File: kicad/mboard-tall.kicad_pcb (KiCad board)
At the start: 2 copper layers, 50.8 x 25.4 mm, 10 parts

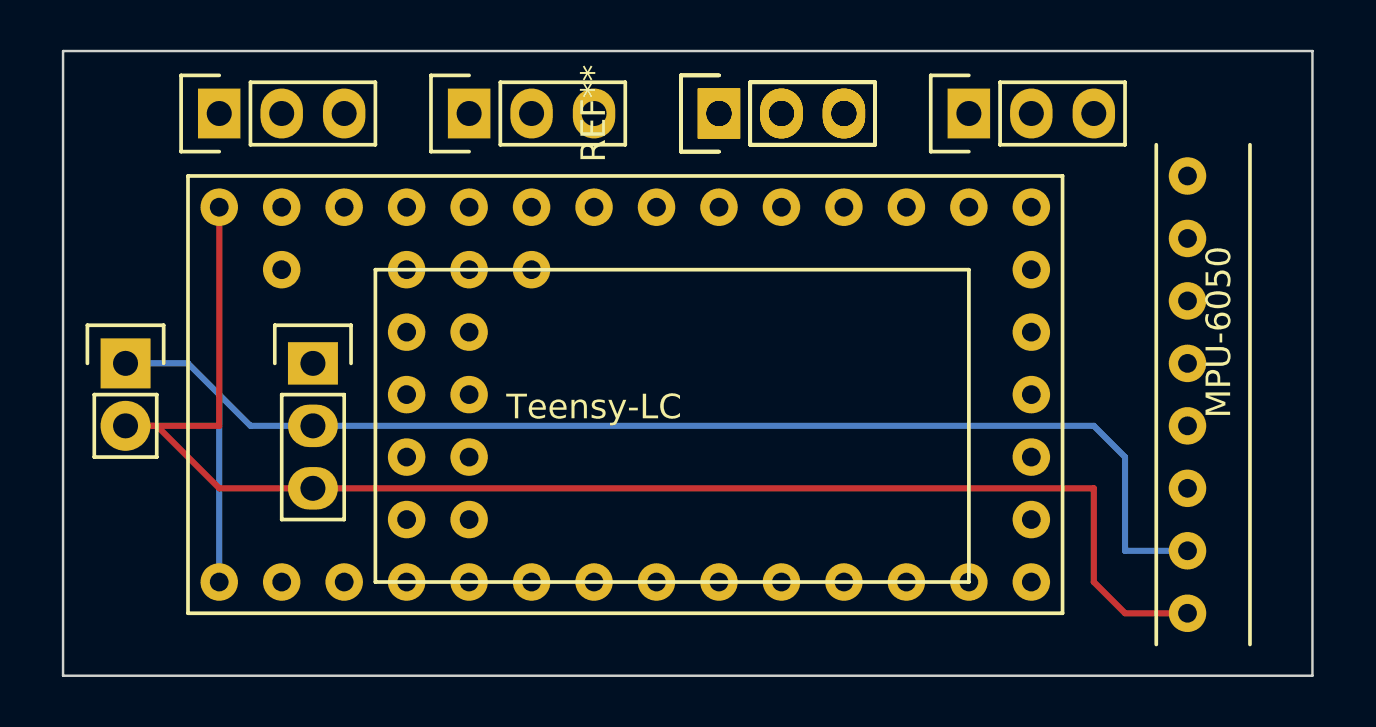
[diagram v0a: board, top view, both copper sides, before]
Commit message: connecting LEDs
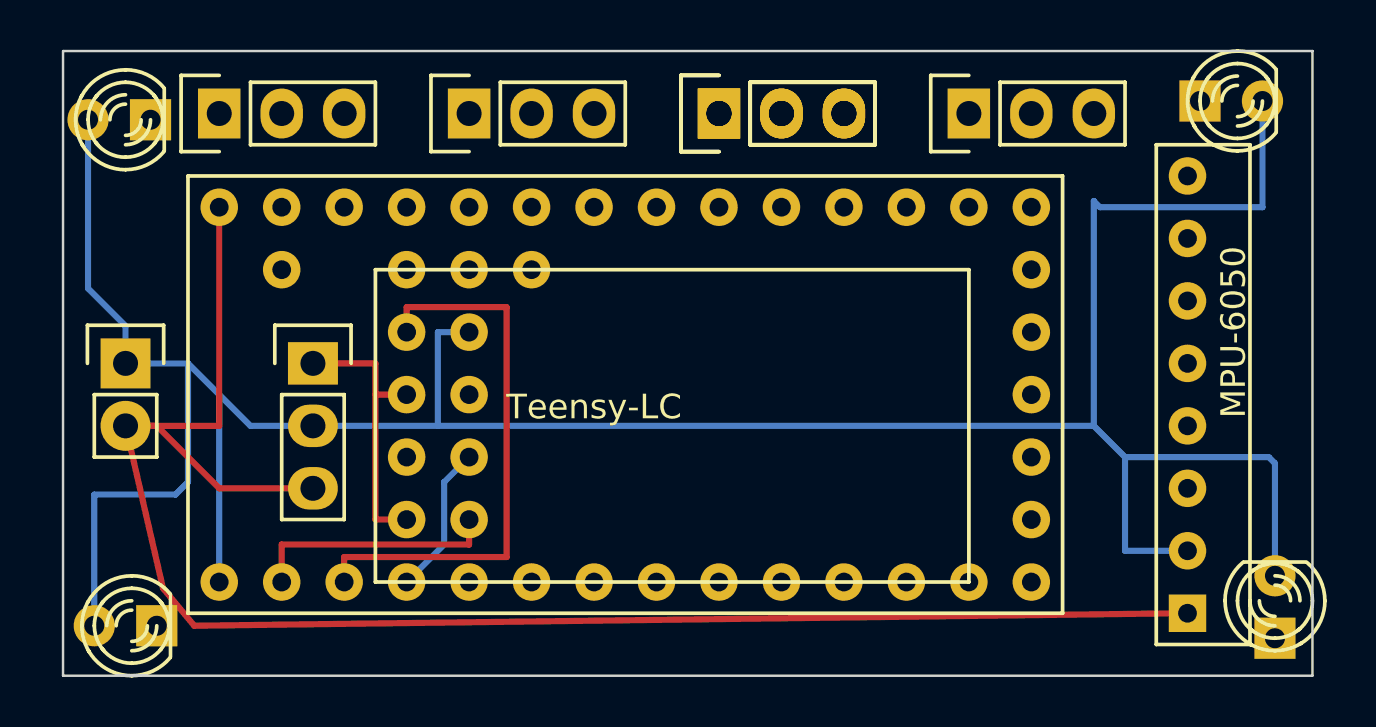
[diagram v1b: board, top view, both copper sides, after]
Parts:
- added REF**: LED-D, LEDs:LED-3MM, F.Cu at (73.4, 56.9)
- added REF**: LED-C, LEDs:LED-3MM, F.Cu at (26.7, 57.7)
- added REF**: LED-B, LEDs:LED-3MM, F.Cu at (26.4, 37.1)
- added REF**: LED-A, LEDs:LED-3MM, F.Cu at (71.6, 36.3)
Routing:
- net (no net): track 117.5 -> 238.0 mm

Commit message: all wird
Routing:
- net (no net): track 238.0 -> 487.3 mm

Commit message: labels and such
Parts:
- LDO33: renamed from REF**; value Pin_Header_Straight_1x03 -> 3.3v
- renumbered REF** to 5V
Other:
- board text added: "PlugCopter 2015-March donpark.org"

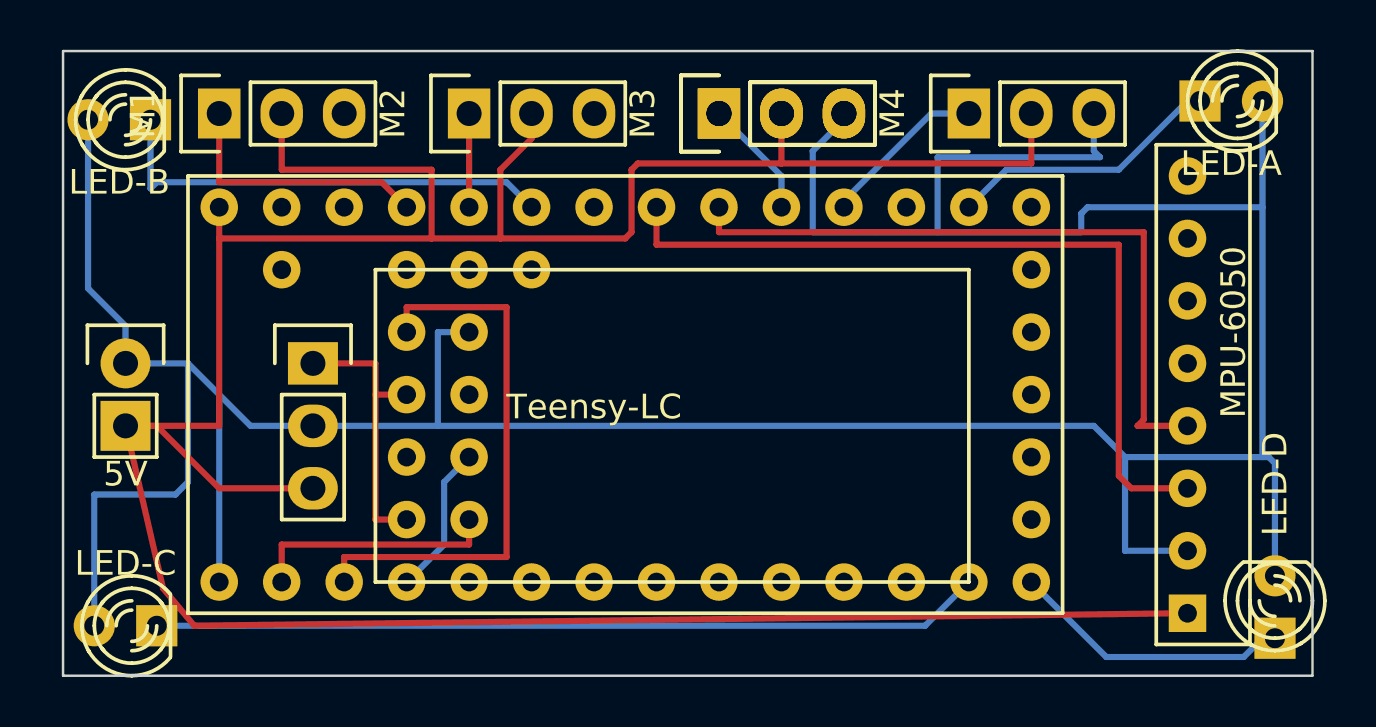
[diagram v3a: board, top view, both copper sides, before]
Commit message: fix trace collision and some labels
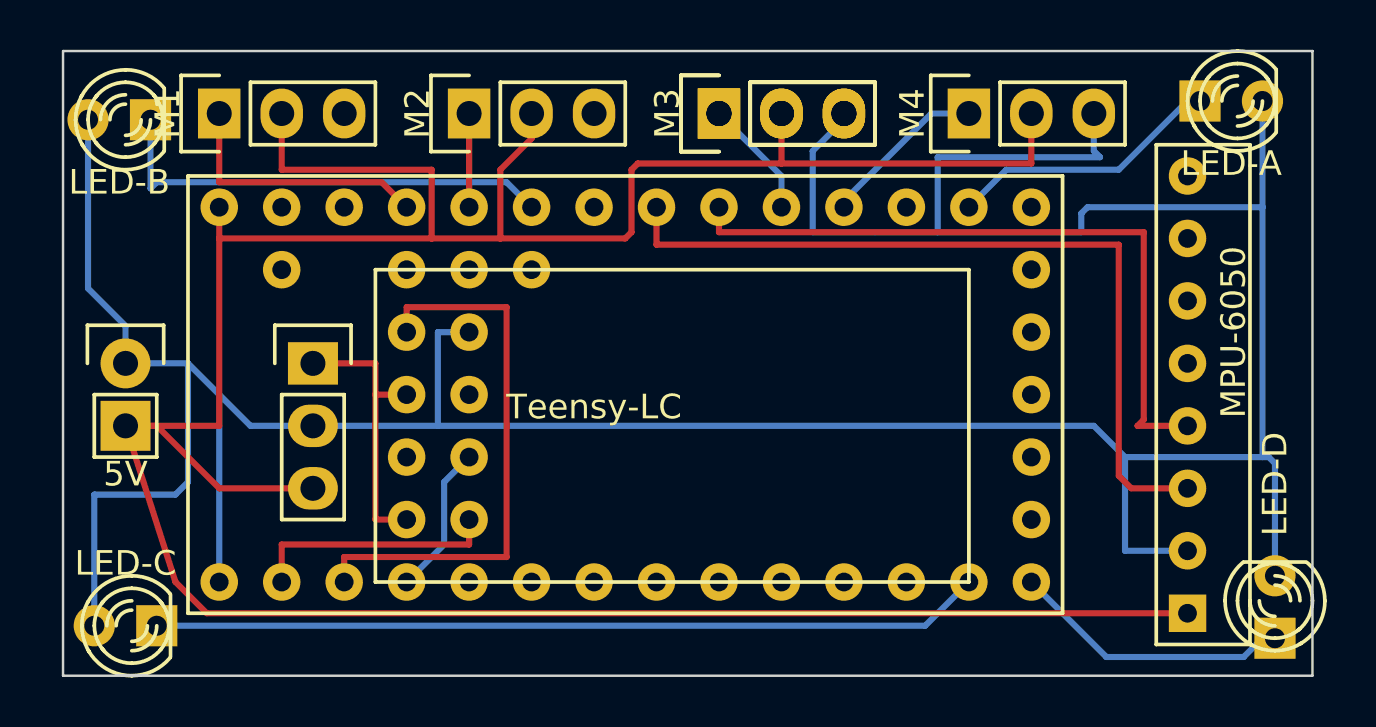
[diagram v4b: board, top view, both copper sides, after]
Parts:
- 5V: value Pin_Header_Straight_1x02 -> (none)
- REF**: value Pin_Header_Straight_1x03 -> (none)
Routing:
- net (no net): track 487.3 -> 486.5 mm
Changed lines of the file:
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@@
-(kicad_pcb (version 4) (host pcbnew 0.201503190816+5525~22~ubuntu14.10.1-product)
+(kicad_pcb (version 4) (host pcbnew "(after 2015-mar-04 BZR unknown)-product")
   (general
     (links 0)
     (no_connects 0)
-    (area 16.680713 32.403 76.157191 59.965001)
+    (area 21.914524 32.403 76.157191 59.965001)
     (thickness 1.6)
     (drawings 5)
@@
   (layers
     (0 F.Cu signal)
-    (31 B.Cu signal)
+    (31 B.Cu signal hide)
     (32 B.Adhes user)
     (33 F.Adhes user)
@@
     (pad_to_mask_clearance 0)
     (aux_axis_origin 0 0)
-    (visible_elements FFFFF77F)
+    (visible_elements 7FFFFFFF)
     (pcbplotparams
       (layerselection 0x010f0_80000001)
@@
       (effects (font (size 1 1) (thickness 0.15)))
     )
-    (fp_text value M4 (at 0 -3.1 90) (layer F.SilkS)
+    (fp_text value M4 (at 0 -2.3 90) (layer F.SilkS)
       (effects (font (size 1 1) (thickness 0.15)))
     )
@@
       (effects (font (size 1 1) (thickness 0.15)))
     )
-    (fp_text value M3 (at 0 -3.1 90) (layer F.SilkS)
+    (fp_text value M3 (at 0 -2.1 90) (layer F.SilkS)
       (effects (font (size 1 1) (thickness 0.15)))
     )
@@
       (effects (font (size 1 1) (thickness 0.15)))
     )
-    (fp_text value Pin_Header_Straight_1x03 (at 0 -3.1 90) (layer F.Fab) hide
+    (fp_text value "" (at 0 -3.1 90) (layer F.Fab) hide
       (effects (font (size 1 1) (thickness 0.15)))
     )
@@
       (effects (font (size 1 1) (thickness 0.15)))
     )
-    (fp_text value M2 (at 0 -3.1 90) (layer F.SilkS)
+    (fp_text value M2 (at 0 -2.1 90) (layer F.SilkS)
       (effects (font (size 1 1) (thickness 0.15)))
     )
@@
       (effects (font (size 1 1) (thickness 0.15)))
     )
-    (fp_text value Pin_Header_Straight_1x02 (at 0 -3.1) (layer F.Fab) hide
+    (fp_text value "" (at 0 -3.1) (layer F.Fab) hide
       (effects (font (size 1 1) (thickness 0.15)))
     )
@@
       (effects (font (size 1 1) (thickness 0.15)))
     )
-    (fp_text value M1 (at 0 -3.1 90) (layer F.SilkS)
+    (fp_text value M1 (at 0 -2.1 90) (layer F.SilkS)
       (effects (font (size 1 1) (thickness 0.15)))
     )
@@
   (segment (start 33.02 54.356) (end 33.02 55.88) (width 0.25) (layer F.Cu) (net 0) (status 20))
   (segment (start 40.64 54.356) (end 33.02 54.356) (width 0.25) (layer F.Cu) (net 0))
-  (segment (start 26.67 49.53) (end 28.194 56.134) (width 0.25) (layer F.Cu) (net 0) (status 10))
-  (segment (start 29.464 57.658) (end 69.596 57.15) (width 0.25) (layer F.Cu) (net 0) (status 20))
-  (segment (start 28.194 56.134) (end 29.464 57.658) (width 0.25) (layer F.Cu) (net 0))
+  (segment (start 26.67 49.53) (end 28.702 55.88) (width 0.25) (layer F.Cu) (net 0) (status 400010))
+  (segment (start 29.972 57.15) (end 69.596 57.15) (width 0.25) (layer F.Cu) (net 0) (status 20))
+  (segment (start 28.702 55.88) (end 29.972 57.15) (width 0.25) (layer F.Cu) (net 0))
   (segment (start 36.83 48.26) (end 38.1 48.26) (width 0.25) (layer F.Cu) (net 0) (status 20))
   (segment (start 34.29 46.99) (end 36.83 46.99) (width 0.25) (layer F.Cu) (net 0) (status 10))

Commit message: Fix the PAD diameters
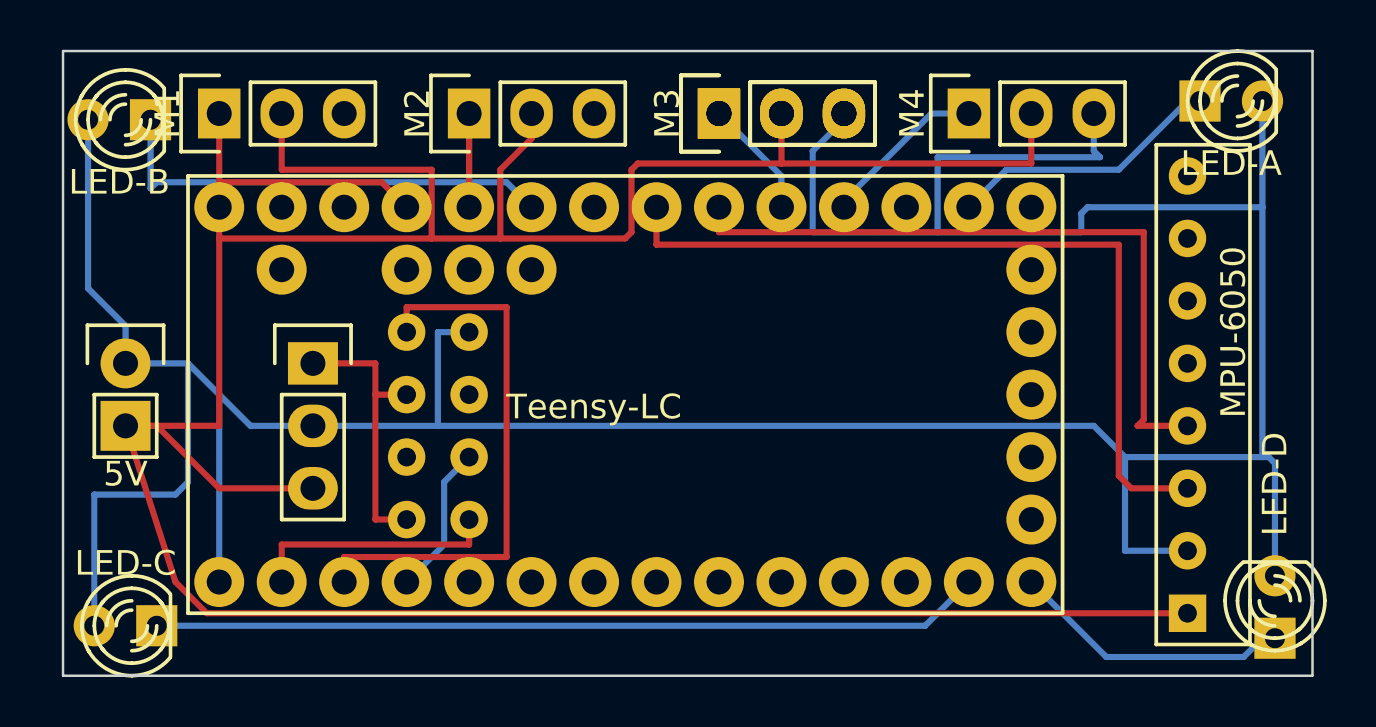
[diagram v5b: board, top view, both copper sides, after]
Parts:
- ESP8266: moved to B.Cu
- moved ESP8266 2.54 mm to (50.8, 48.3)

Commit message: reroute due to wider via
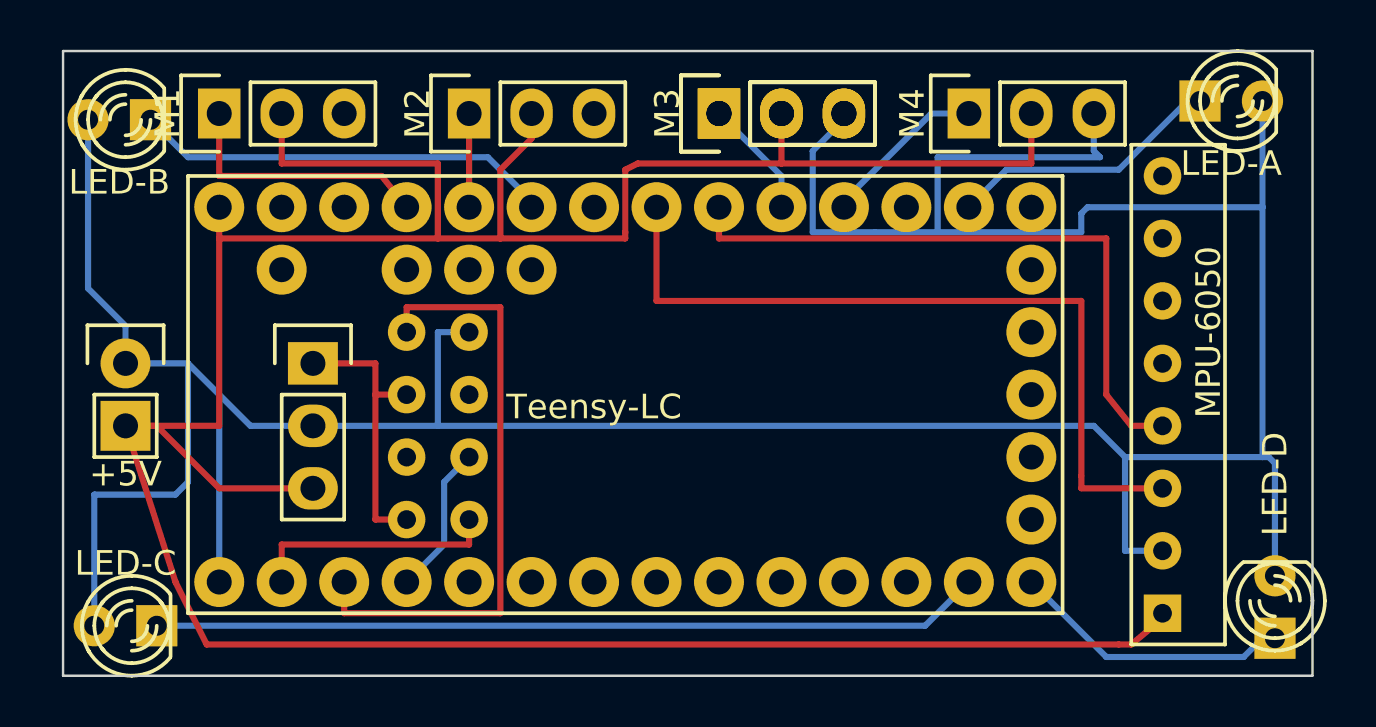
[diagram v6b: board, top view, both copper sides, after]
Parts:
- moved MPU-6050 1.02 mm to (73.9, 49.5)
- renumbered 5V to +5V, REF** to ?
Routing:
- net (no net): track 486.5 -> 484.4 mm
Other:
- board text added: "+"
- board text added: "-"
- board text added: "PlugCopter 2015-Apr donpark.org"
- board text removed: "PlugCopter 2015-March donpark.org"
